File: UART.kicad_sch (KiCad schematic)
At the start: 10 parts, among them J9 430450612, T1 DA2304-ALD, U4 ISO3086TDWR, U5 MAX485, U6 LP2985A-50DBVR

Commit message: Adding Libraries
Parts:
- removed U4: ISO3086TDWR, ISO3086TDWR:SOIC127P1030X265-16N, symbol ISO3086TDWR:ISO3086TDWR
- added C1, C3, C7: 10uF, symbol Device:C
- added C10, C8: 0.1uF, symbol Device:C
- added C11: 10nF, symbol Device:C
- added C2, C9: 4.7uF, symbol Device:C
- added D3, D9: MBR0520LT, Diode_SMD:D_SOD-123, symbol Diode:MBR0520LT
- added J19: 430450212, CON_430450212_MOL, symbol 0430450212:430450212
- added U9: ISO3086TDW, ISO3086TDW:SOIC127P1030X265-16N, symbol ISO3086TDW:ISO3086TDW
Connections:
- net +5V: now also T1.2, T1.3, C1.2, C2.1, C3.1, U9.4 (VCC1); no longer J9.1, J9.2, R10.1, R5.1, R7.1, R8.1, U5.5 (GND), U5.8 (VCC)
- net GND: now also C1.1, C2.2, C3.2, U9.3 (GND1)
- net RX: now also U9.5 (R)
- net TX: now also U9.8 (D)
- net at U6.1 (VIN): now also U6.3 (ON/*OFF), C7.2, C8.2, D3.1 (K), D9.1 (K)
- net GND_TB: now reaches U6.2 (GND)
- net GND_TB: now also T1.6, T1.7, U6.5 (VOUT), C10.1, C10.2, C11.2, C7.1, C8.1, C9.1, C9.2, U9.15 (GND2), U9.16 (VCC2), U9.9 (GND2)
- net at U6.4 (BYPASS): now also C11.1
- net at T1.1: now also U9.1 (D1)
- net at T1.4: now also U9.2 (D2)
- net at T1.5: now also D9.2 (A)
- net at T1.8: now also D3.2 (A)
- net GPIO_13 renamed BKP_EN
- new net: J19.2, U9.11 (Y), U9.14 (A)
- new net: J19.1, U9.12 (Z), U9.13 (B)
- new net 5V_BACKPLANE: J9.1, J9.2, R10.1, R5.1, R7.1, R8.1, U5.5 (GND), U5.8 (VCC)
- new net TB_EN: U9.6 (~{RE}), U9.7 (DE)
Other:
- moved on the sheet: J9, R10, R11, R5, R7, R8, T1, U5, U6

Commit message: Finalizing Schematic
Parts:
- added C14: 0.1uF, symbol Device:C
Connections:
- net 5V_BACKPLANE: now also C14.2
- net GND: now also C14.1
- net at J19.2, U9.14 (A): no longer U9.11 (Y)
- net at J19.1, U9.13 (B): no longer U9.12 (Z)
- no-connect marks 0 -> 2
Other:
- note added: "B_TB A_TB"
- moved on the sheet: C1, C10, C11, C2, C3, C7, C8, C9, D3, D9, J19, J9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

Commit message: Final Schematic Update
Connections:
- net GND_TB: no longer C10.2, C9.2, U6.5 (VOUT), U9.16 (VCC2)
- net at U9.11 (Y): now also J19.2, U9.14 (A)
- net at U9.12 (Z): now also J19.1, U9.13 (B)
- new net: C10.2, C9.2, U6.5 (VOUT), U9.16 (VCC2)
- no-connect marks 2 -> 0
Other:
- moved on the sheet: C1, C10, C11, C14, C2, C3, C7, C8, C9, D3, D9, J19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

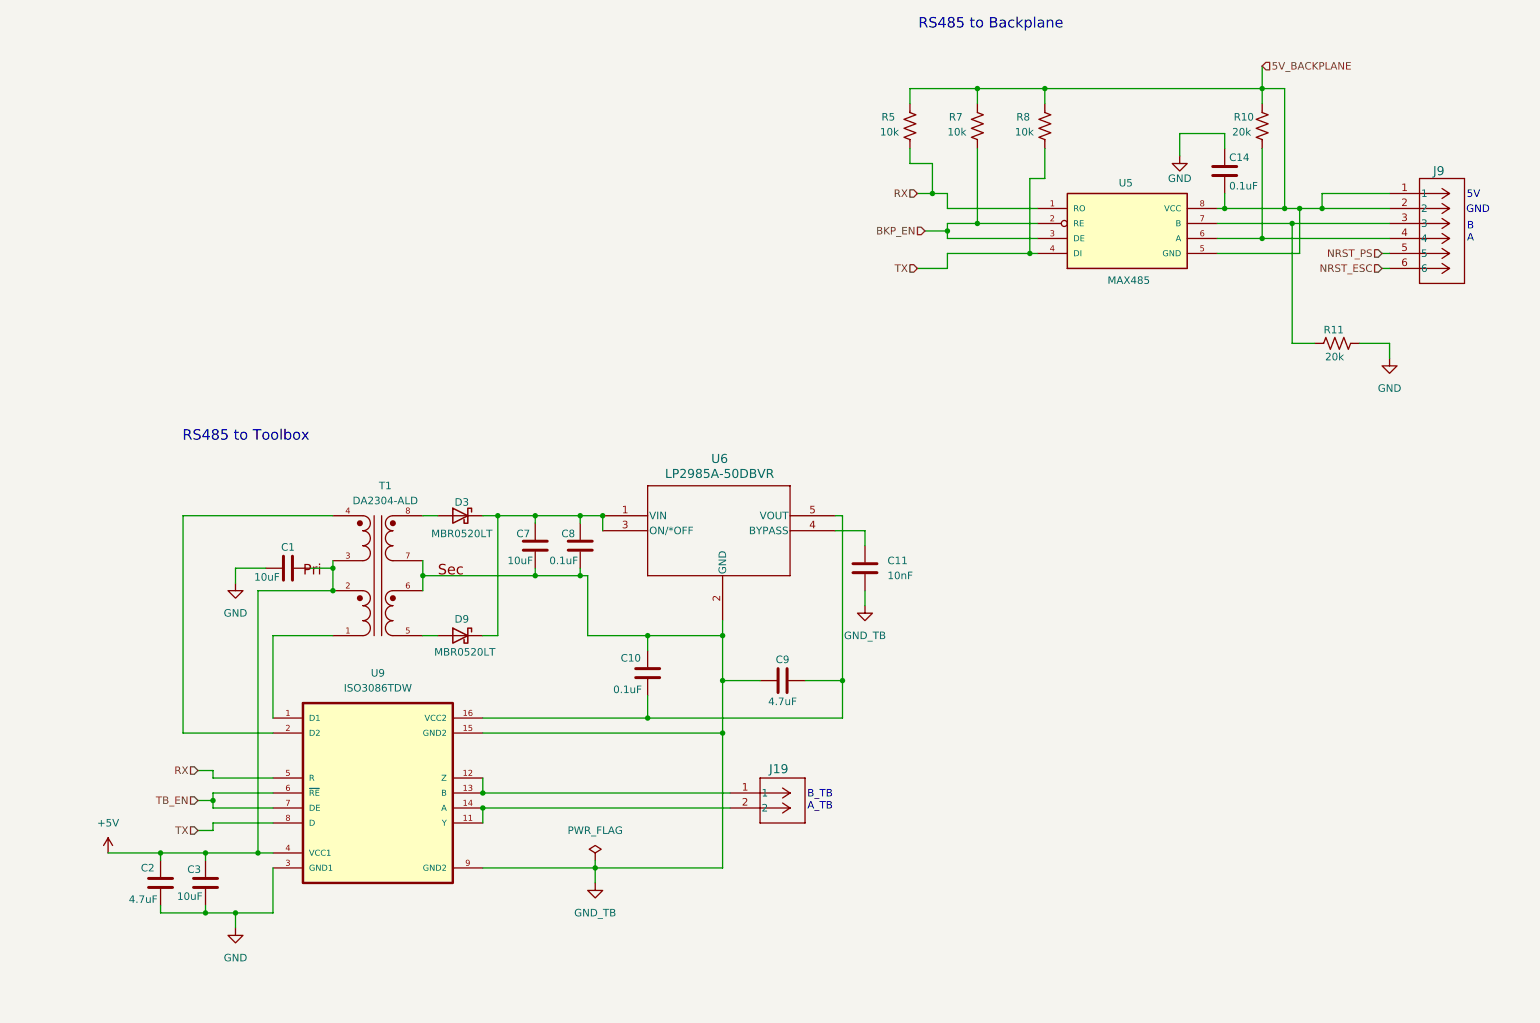
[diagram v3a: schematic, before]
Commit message: Sensor Connector Update
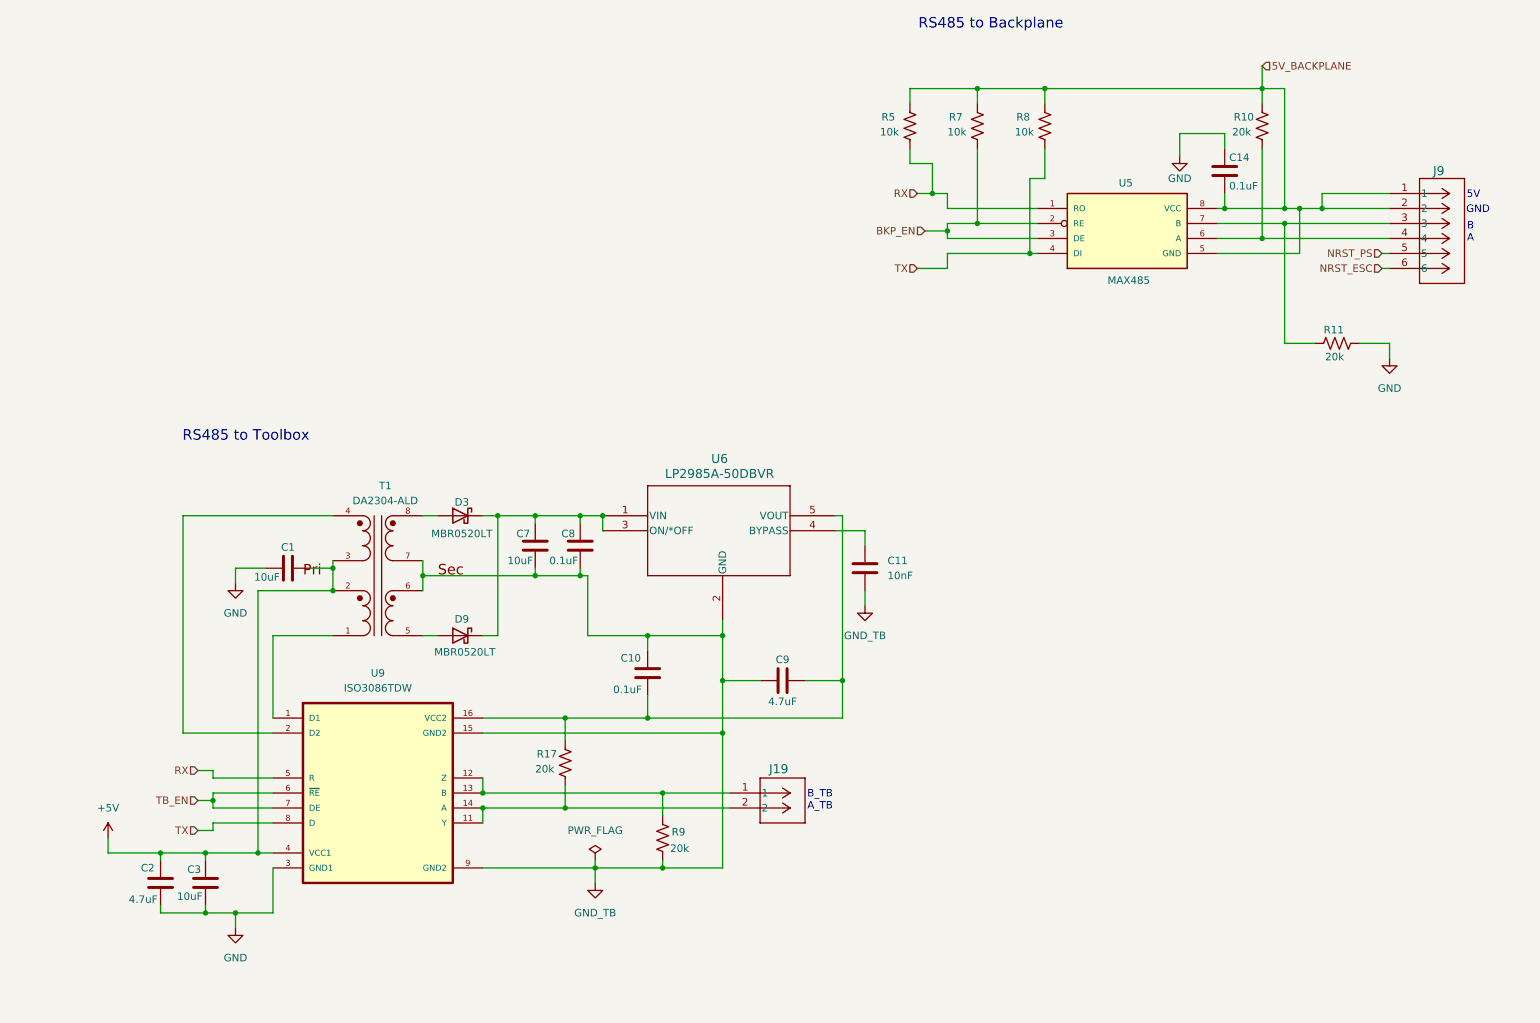
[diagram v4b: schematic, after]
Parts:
- added R17, R9: 20k, symbol Device:R_US
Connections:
- net GND_TB: now also R9.2
- net at C10.2, C9.2, U6.5 (VOUT)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: now also R17.1
- net at J19.2, U9.11 (Y), U9.14 (A): now also R17.2
- net at J19.1, U9.12 (Z), U9.13 (B): now also R9.1

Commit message: Pre-Toolbox Final
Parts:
- C1, C10, C11, C14, C2, C3, C7, C8, C9: footprint (none) -> Capacitor_SMD:C_0805_2012Metric_Pad1.18x1.45mm_HandSolder
- D3, D9: footprint Diode_SMD:D_SOD-123 -> (none)
- J19: footprint CON_430450212_MOL -> 0430450212/:CON_430450212_MOL
- J9: footprint CON_430450612_MOL -> CON_430450612_MOL:CON_430450612_MOL
- R10, R11: value 20k -> 10k; footprint (none) -> Resistor_SMD:R_0805_2012Metric_Pad1.20x1.40mm_HandSolder
- R17, R5, R7, R8, R9: footprint (none) -> Resistor_SMD:R_0805_2012Metric_Pad1.20x1.40mm_HandSolder
- U5: footprint (none) -> MAX485:SO08
- U6: footprint DBV5 -> (none)
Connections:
- net RX: no longer U9.5 (R)
- net TX: no longer U9.8 (D)
- new net RX_TB: U9.5 (R)
- new net TX_TB: U9.8 (D)
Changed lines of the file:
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@@
+		)
+	)
+	(hierarchical_label "TX_TB"
+		(shape input)
+		(at 57.15 160.02 180)
+		(fields_autoplaced yes)
+		(effects
+			(font
+				(size 1.27 1.27)
+			)
+			(justify right)
+		)
+	)
+	(hierarchical_label "RX_TB"
+		(shape input)
+		(at 57.15 149.86 180)
+		(fields_autoplaced yes)
+		(effects
+			(font
+				(size 1.27 1.27)
+			)
+			(justify right)
 		)
 	)
@@
 		)
 	)
-	(hierarchical_label "TX"
-		(shape input)
-		(at 57.15 160.02 180)
-		(fields_autoplaced yes)
-		(effects
-			(font
-				(size 1.27 1.27)
-			)
-			(justify right)
-		)
-	)
-	(hierarchical_label "RX"
-		(shape input)
-		(at 57.15 149.86 180)
-		(fields_autoplaced yes)
-		(effects
-			(font
-				(size 1.27 1.27)
-			)
-			(justify right)
-		)
-	)
 	(hierarchical_label "NRST_PS"
 		(shape input)
@@
 			)
 		)
-		(property "Footprint" "Diode_SMD:D_SOD-123"
+		(property "Footprint" ""
 			(at 101.6 131.445 0)
 			(effects
@@
 			)
 		)
-		(property "Footprint" ""
+		(property "Footprint" "Capacitor_SMD:C_0805_2012Metric_Pad1.18x1.45mm_HandSolder"
 			(at 76.2 116.5352 0)
 			(effects
@@
 			)
 		)
-		(property "Footprint" ""
+		(property "Footprint" "Capacitor_SMD:C_0805_2012Metric_Pad1.18x1.45mm_HandSolder"
 			(at 122.8852 107.95 0)
 			(effects
@@
 			)
 		)
-		(property "Footprint" "DBV5"
+		(property "Footprint" ""
 			(at 123.698 104.394 0)
 			(effects
@@
 			)
 		)
-		(property "Footprint" "Diode_SMD:D_SOD-123"
+		(property "Footprint" ""
 			(at 101.6 111.125 0)
 			(effects
@@
 			)
 		)
-		(property "Footprint" ""
+		(property "Footprint" "Resistor_SMD:R_0805_2012Metric_Pad1.20x1.40mm_HandSolder"
 			(at 136.906 161.544 90)
 			(effects
@@
 			)
 		)
-		(property "Value" "20k"
+		(property "Value" "10k"
 			(at 232.41 41.656 0)
 			(effects
@@
 			)
 		)
-		(property "Footprint" ""
+		(property "Footprint" "Resistor_SMD:R_0805_2012Metric_Pad1.20x1.40mm_HandSolder"
 			(at 238.506 40.894 90)
 			(effects
@@
 			)
 		)
-		(property "Footprint" ""
+		(property "Footprint" "Capacitor_SMD:C_0805_2012Metric_Pad1.18x1.45mm_HandSolder"
 			(at 49.8348 172.72 0)
 			(effects
@@
 			)
 		)
-		(property "Value" "20k"
+		(property "Value" "10k"
 			(at 248.158 79.756 90)
 			(effects
@@
 			)
 		)
-		(property "Footprint" ""
+		(property "Footprint" "Resistor_SMD:R_0805_2012Metric_Pad1.20x1.40mm_HandSolder"
 			(at 249.936 78.486 90)
 			(effects
@@
 			)
 		)
-		(property "Footprint" ""
+		(property "Footprint" "Resistor_SMD:R_0805_2012Metric_Pad1.20x1.40mm_HandSolder"
 			(at 201.676 40.894 90)
 			(effects
@@
 			)
 		)
-		(property "Footprint" "CON_430450612_MOL"
+		(property "Footprint" "CON_430450612_MOL:CON_430450612_MOL"
 			(at 259.08 52.07 0)
 			(effects
@@
 			)
 		)
-		(property "Footprint" ""
+		(property "Footprint" "Capacitor_SMD:C_0805_2012Metric_Pad1.18x1.45mm_HandSolder"
 			(at 171.1452 119.38 0)
 			(effects
@@
 			)
 		)
-		(property "Footprint" ""
+		(property "Footprint" "Capacitor_SMD:C_0805_2012Metric_Pad1.18x1.45mm_HandSolder"
 			(at 134.3152 137.16 0)
 			(effects
@@
 			)
 		)
-		(property "Footprint" ""
+		(property "Footprint" "Resistor_SMD:R_0805_2012Metric_Pad1.20x1.40mm_HandSolder"
 			(at 120.396 148.844 90)
 			(effects
@@
 			)
 		)
-		(property "Footprint" ""
+		(property "Footprint" "MAX485:SO08"
 			(at 214.63 59.69 0)
 			(effects
@@
 			)
 		)
-		(property "Footprint" ""
+		(property "Footprint" "Capacitor_SMD:C_0805_2012Metric_Pad1.18x1.45mm_HandSolder"
 			(at 57.4548 172.72 0)
 			(effects
@@
 			)
 		)
-		(property "Footprint" ""
+		(property "Footprint" "Resistor_SMD:R_0805_2012Metric_Pad1.20x1.40mm_HandSolder"
 			(at 190.246 40.894 90)
 			(effects
@@
 			)
 		)
-		(property "Footprint" ""
+		(property "Footprint" "Capacitor_SMD:C_0805_2012Metric_Pad1.18x1.45mm_HandSolder"
 			(at 115.2652 107.95 0)
 			(effects
@@
 			)
 		)
-		(property "Footprint" ""
+		(property "Footprint" "Resistor_SMD:R_0805_2012Metric_Pad1.20x1.40mm_HandSolder"
 			(at 178.816 40.894 90)
 			(effects
@@
 			)
 		)
-		(property "Footprint" "CON_430450212_MOL"
+		(property "Footprint" "0430450212/:CON_430450212_MOL"
 			(at 147.32 153.67 0)
 			(effects
@@
 			)
 		)
-		(property "Footprint" ""
+		(property "Footprint" "Capacitor_SMD:C_0805_2012Metric_Pad1.18x1.45mm_HandSolder"
 			(at 232.1052 52.07 0)
 			(effects
@@
 			)
 		)
-		(property "Footprint" ""
+		(property "Footprint" "Capacitor_SMD:C_0805_2012Metric_Pad1.18x1.45mm_HandSolder"
 			(at 160.02 133.6548 0)
 			(effects

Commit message: Finalized Footprints
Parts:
- removed C11: 10nF, Capacitor_SMD:C_0805_2012Metric_Pad1.18x1.45mm_HandSolder, symbol Device:C
- removed D3, D9: MBR0520LT, symbol Diode:MBR0520LT
- removed J19: 430450212, 0430450212/:CON_430450212_MOL, symbol 0430450212:430450212
- removed J9: 430450612, CON_430450612_MOL:CON_430450612_MOL, symbol CON_430450612_MOL:430450612
- removed R7, R8: 10k, Resistor_SMD:R_0805_2012Metric_Pad1.20x1.40mm_HandSolder, symbol Device:R_US
- removed T1: DA2304-ALD, DA2304-ALD:XFMR_DA2304-ALD, symbol DA2304-ALD:DA2304-ALD
- removed U6: LP2985A-50DBVR, symbol LP2985A-50DBVR:LP2985A-50DBVR
- removed U9: ISO3086TDW, ISO3086TDW:SOIC127P1030X265-16N, symbol ISO3086TDW:ISO3086TDW
- added C4: 10uF, Capacitor_SMD:C_0603_1608Metric_Pad1.08x0.95mm_HandSolder, symbol Device:C
- added C6: 1uF, Capacitor_SMD:C_0603_1608Metric_Pad1.08x0.95mm_HandSolder, symbol Device:C
- added FB1, FB2, FB3, FB4, FB5: FerriteBead, BLM18KN331EH1D:BLM18_MUR-M, symbol Device:FerriteBead
- added J22, J24: 430450212, 0430450212/:CON_430450212_MOL, symbol 0430450212:430450212
- added J23: 430450612, CON_430450612_MOL:CON_430450612_MOL, symbol CON_430450612_MOL:430450612
- added R19, R20: 10k, Resistor_SMD:R_0603_1608Metric_Pad0.98x0.95mm_HandSolder, symbol Device:R_US
- added U7: ISOW1432BDFMR, ISOW1432BDFMR:SOIC127P1030X355-20N, symbol ISOW1432BDFMR:ISOW1432BDFMR
- C1, C10, C14, C8: footprint Capacitor_SMD:C_0805_2012Metric_Pad1.18x1.45mm_HandSolder -> Capacitor_SMD:C_0603_1608Metric_Pad1.08x0.95mm_HandSolder
- C2: value 4.7uF -> 1uF; footprint Capacitor_SMD:C_0805_2012Metric_Pad1.18x1.45mm_HandSolder -> Capacitor_SMD:C_0603_1608Metric_Pad1.08x0.95mm_HandSolder
- C3, C7: value 10uF -> 10nF; footprint Capacitor_SMD:C_0805_2012Metric_Pad1.18x1.45mm_HandSolder -> Capacitor_SMD:C_0603_1608Metric_Pad1.08x0.95mm_HandSolder
- C9: value 4.7uF -> 10uF; footprint Capacitor_SMD:C_0805_2012Metric_Pad1.18x1.45mm_HandSolder -> Capacitor_SMD:C_0603_1608Metric_Pad1.08x0.95mm_HandSolder
- R10, R11: footprint Resistor_SMD:R_0805_2012Metric_Pad1.20x1.40mm_HandSolder -> Resistor_SMD:R_0603_1608Metric_Pad0.98x0.95mm_HandSolder
- R17: value 20k -> 120; footprint Resistor_SMD:R_0805_2012Metric_Pad1.20x1.40mm_HandSolder -> Resistor_SMD:R_0603_1608Metric_Pad0.98x0.95mm_HandSolder
- R5: value 10k -> 120; footprint Resistor_SMD:R_0805_2012Metric_Pad1.20x1.40mm_HandSolder -> Resistor_SMD:R_0603_1608Metric_Pad0.98x0.95mm_HandSolder
- R9: value 20k -> 5k; footprint Resistor_SMD:R_0805_2012Metric_Pad1.20x1.40mm_HandSolder -> Resistor_SMD:R_0603_1608Metric_Pad0.98x0.95mm_HandSolder
- U5: footprint MAX485:SO08 -> AZ1117IH_3_3TRG1:SOT223_AZ1117I_6P5X3P5_DIO-M
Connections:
- net +5V: now also R10.1, FB4.1; no longer C1.2, C2.1, C3.1
- net 5V_BACKPLANE: now also J23.1; no longer C14.2, R10.1, R5.1, U5.5 (GND), U5.8 (VCC)
- net GND: now also C10.1, R11.2, U5.5 (GND), FB5.1, J23.2, U7.6 (GNDIO); no longer C1.1, C2.2, C3.2, R11.1
- net GND_TB: now also C8.2, C9.2, FB3.1, J23.6, R19.2, U7.15 (GISOIN); no longer C10.1, C7.1, C8.1, C9.1, R9.2
- net NRST_ESC: now also J23.4
- net NRST_PS: now also J23.3
- net RX: no longer R5.2
- net RX_TB: now also U7.4 (R)
- net TB_EN: now also U7.3 (DE), U7.5 (~{RE})
- net TX_TB: now also U7.2 (D)
- net at C7.2: now also C4.2, C6.2, FB3.2, U7.11 (GND2), U7.13 (MODE); no longer C8.2
- net ISO_FLT: now reaches R9.1
- net ISO_FLT: now also U7.8 (EN/FLT)
- net at R10.2, U5.6 (A): now also C14.2, R5.2, U5.8 (VCC), J24.2
- net at U5.7 (B): now also R11.1, R5.1, J24.1; no longer R11.2
- net at R17.2: now also J22.2, R20.1, U7.17 (Y), U7.20 (A)
- new net: C4.1, C6.1, C7.1, FB2.1, U7.12 (VISOOUT)
- new net: C10.2, FB1.2, R9.2, U7.1 (VIO)
- new net: C1.1, C2.1, C3.1, FB4.2, U7.9 (VDD)
- new net: C1.2, C2.2, C3.2, FB5.2, U7.10 (GND1)
- new net: J22.1, R17.1, R19.1, U7.18 (Z), U7.19 (B)
- new net +3V3: FB1.1
- new net +5V_TB: C8.1, C9.1, FB2.2, R20.2, U7.16 (VISOIN)
- new net NRST_TB: J23.5
- no-connect marks 0 -> 2
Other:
- note added: "Backplane GPIO and Power Connector"
- note added: "NRST_PS NRST_ESC"
- note added: "NRST_TB GND_TB"
- moved on the sheet: C14, R10, R11, U5

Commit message: Updating 3d Models
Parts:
- U5: footprint AZ1117IH_3_3TRG1:SOT223_AZ1117I_6P5X3P5_DIO-M -> MAX485:SO08
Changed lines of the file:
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@@
 			)
 		)
-		(property "Footprint" "AZ1117IH_3_3TRG1:SOT223_AZ1117I_6P5X3P5_DIO-M"
+		(property "Footprint" "MAX485:SO08"
 			(at 222.25 110.49 0)
 			(effects
